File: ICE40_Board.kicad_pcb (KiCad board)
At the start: 4 copper layers, 62.5 x 26.7 mm, 40 parts, among them J1 SPI, J2 EXPANSION, J3 R_HDR, J4 L_HDR, U1 AZ1117-1.2, U2 AMS1117-3.3, U3 USB4110-GF-A, U4 iCE40HX1K-VQ100, U5 FT2232HQ, U6 93LCxxC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

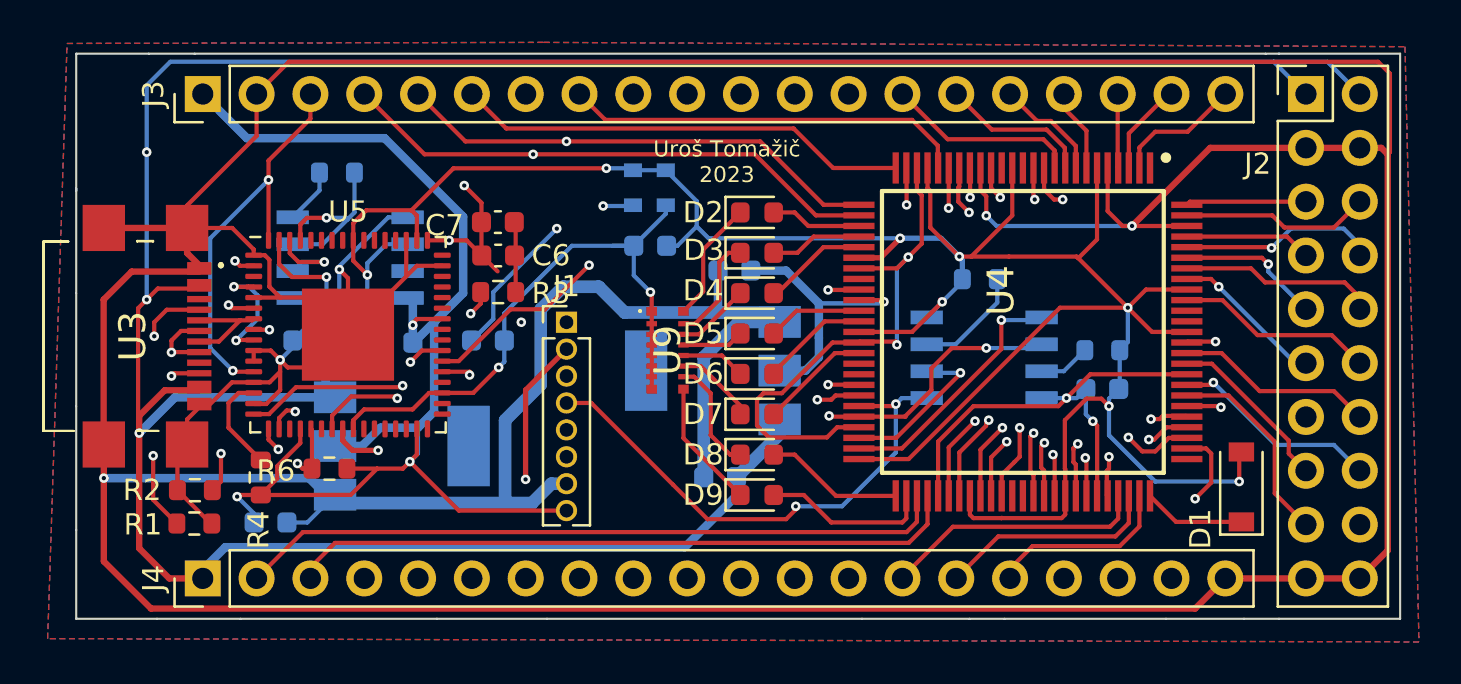
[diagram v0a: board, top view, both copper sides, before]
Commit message: added power led
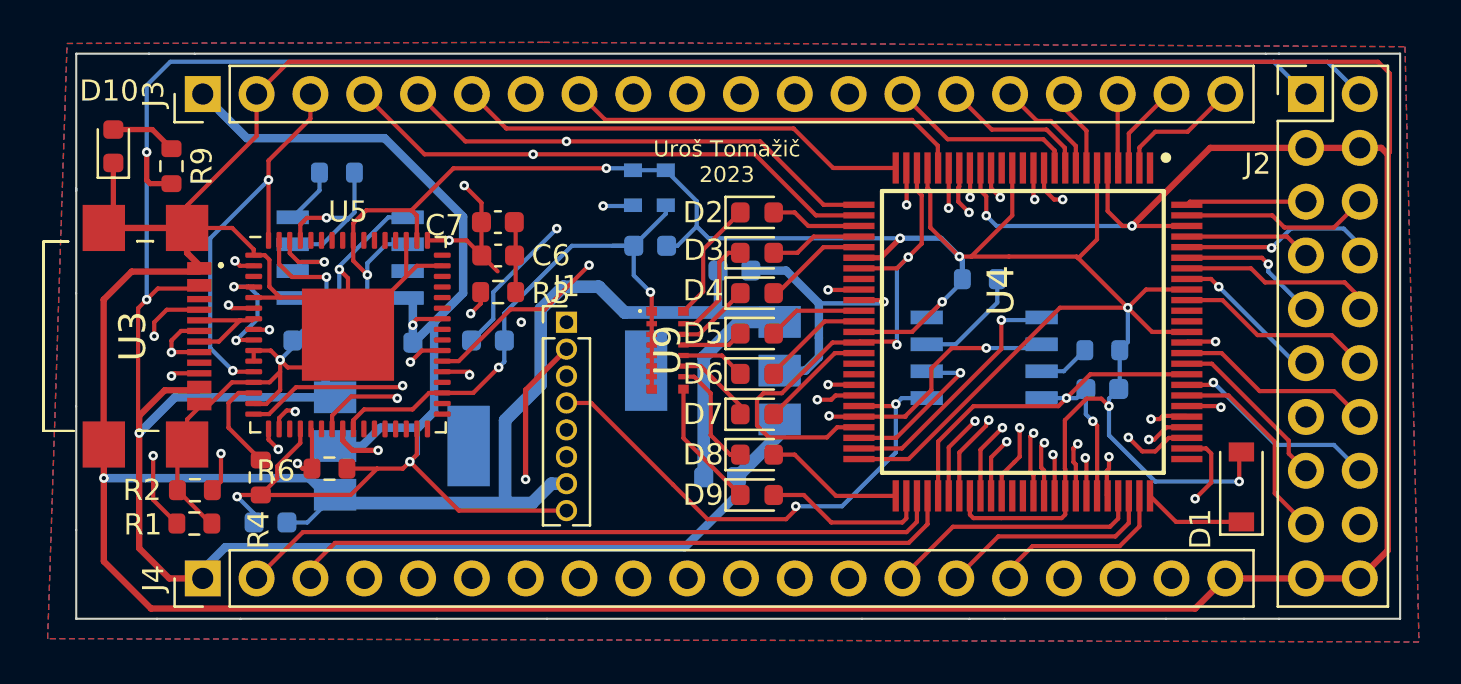
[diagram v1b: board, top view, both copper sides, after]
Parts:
- added D10: LED, LED_SMD:LED_0603_1608Metric, F.Cu at (68.9, 46.2)
- added R9: 330R, Resistor_SMD:R_0603_1608Metric, F.Cu at (71.7, 47.1)
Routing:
- net GND: track 413.6 -> 416.8 mm
- net Net-(D10-Pad2): track 0.00 -> 3.12 mm
- net +5V: track 164.3 -> 166.8 mm
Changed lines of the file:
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@@
   (net 131 "unconnected-(U6-Pad7)")
   (net 132 "Net-(C6-Pad2)")
+  (net 133 "Net-(D10-Pad2)")
   (footprint "Diode_SMD:D_SOD-123" (layer "F.Cu")
     (at 122.174 62.23 90)
@@
     )
   )
+  (footprint "Resistor_SMD:R_0603_1608Metric" (layer "F.Cu")
+    (at 71.6788 47.0916 -90)
+    (descr "Resistor SMD 0603 (1608 Metric), square (rectangular) end terminal, IPC_7351 nominal, (Body size source: IPC-SM-782 page 72, https://www.pcb-3d.com/wordpress/wp-content/uploads/ipc-sm-782a_amendment_1_and_2.pdf), generated with kicad-footprint-generator")
+    (tags "resistor")
+    (property "Sheetfile" "ICE40_Board.kicad_sch")
+    (property "Sheetname" "")
+    (attr smd)
+    (fp_text reference "R9" (at 0 -1.43 90) (layer "F.SilkS")
+      (effects (font (size 1 1) (thickness 0.15)))
+    )
+    (fp_text value "330R" (at 0 1.43 90) (layer "F.Fab")
+      (effects (font (size 1 1) (thickness 0.15)))
+    )
+    (fp_text user "${REFERENCE}" (at 0 0 90) (layer "F.Fab")
+      (effects (font (size 0.4 0.4) (thickness 0.06)))
+    )
+    (fp_line (start -0.237258 0.5225) (end 0.237258 0.5225) (layer "F.SilkS") (width 0.12))
+    (fp_line (start -0.237258 -0.5225) (end 0.237258 -0.5225) (layer "F.SilkS") (width 0.12))
+    (fp_line (start 1.48 0.73) (end -1.48 0.73) (layer "F.CrtYd") (width 0.05))
+    (fp_line (start 1.48 -0.73) (end 1.48 0.73) (layer "F.CrtYd") (width 0.05))
+    (fp_line (start -1.48 -0.73) (end 1.48 -0.73) (layer "F.CrtYd") (width 0.05))
+    (fp_line (start -1.48 0.73) (end -1.48 -0.73) (layer "F.CrtYd") (width 0.05))
+    (fp_line (start -0.8 -0.4125) (end 0.8 -0.4125) (layer "F.Fab") (width 0.1))
+    (fp_line (start 0.8 -0.4125) (end 0.8 0.4125) (layer "F.Fab") (width 0.1))
+    (fp_line (start -0.8 0.4125) (end -0.8 -0.4125) (layer "F.Fab") (width 0.1))
+    (fp_line (start 0.8 0.4125) (end -0.8 0.4125) (layer "F.Fab") (width 0.1))
+    (pad "1" smd roundrect (at -0.825 0 270) (size 0.8 0.95) (layers "F.Cu" "F.Paste" "F.Mask") (roundrect_rratio 0.25)
+      (net 133 "Net-(D10-Pad2)") (pintype "passive"))
+    (pad "2" smd roundrect (at 0.825 0 270) (size 0.8 0.95) (layers "F.Cu" "F.Paste" "F.Mask") (roundrect_rratio 0.25)
+      (net 3 "+5V") (pintype "passive"))
+    (model "${KICAD6_3DMODEL_DIR}/Resistor_SMD.3dshapes/R_0603_1608Metric.wrl"
+      (offset (xyz 0 0 0))
+      (scale (xyz 1 1 1))
+      (rotate (xyz 0 0 0))
+    )
+  )
   (footprint "LED_SMD:LED_0603_1608Metric" (layer "F.Cu")
     (at 99.314 62.611)
@@
     )
   )
+  (footprint "LED_SMD:LED_0603_1608Metric" (layer "F.Cu")
+    (at 68.9356 46.1519 90)
+    (descr "LED SMD 0603 (1608 Metric), square (rectangular) end terminal, IPC_7351 nominal, (Body size source: http://www.tortai-tech.com/upload/download/2011102023233369053.pdf), generated with kicad-footprint-generator")
+    (tags "LED")
+    (property "Sheetfile" "ICE40_Board.kicad_sch")
+    (property "Sheetname" "")
+    (attr smd)
+    (fp_text reference "D10" (at 2.6163 -0.2032 180) (layer "F.SilkS")
+      (effects (font (size 1 1) (thickness 0.15)))
+    )
+    (fp_text value "LED" (at 0 1.43 90) (layer "F.Fab")
+      (effects (font (size 1 1) (thickness 0.15)))
+    )
+    (fp_text user "${REFERENCE}" (at 0 0 90) (layer "F.Fab")
+      (effects (font (size 0.4 0.4) (thickness 0.06)))
+    )
+    (fp_line (start -1.485 0.735) (end 0.8 0.735) (layer "F.SilkS") (width 0.12))
+    (fp_line (start 0.8 -0.735) (end -1.485 -0.735) (layer "F.SilkS") (width 0.12))
+    (fp_line (start -1.485 -0.735) (end -1.485 0.735) (layer "F.SilkS") (width 0.12))
+    (fp_line (start -1.48 -0.73) (end 1.48 -0.73) (layer "F.CrtYd") (width 0.05))
+    (fp_line (start 1.48 -0.73) (end 1.48 0.73) (layer "F.CrtYd") (width 0.05))
+    (fp_line (start -1.48 0.73) (end -1.48 -0.73) (layer "F.CrtYd") (width 0.05))
+    (fp_line (start 1.48 0.73) (end -1.48 0.73) (layer "F.CrtYd") (width 0.05))
+    (fp_line (start -0.5 -0.4) (end -0.8 -0.1) (layer "F.Fab") (width 0.1))
+    (fp_line (start -0.8 -0.1) (end -0.8 0.4) (layer "F.Fab") (width 0.1))
+    (fp_line (start 0.8 -0.4) (end -0.5 -0.4) (layer "F.Fab") (width 0.1))
+    (fp_line (start 0.8 0.4) (end 0.8 -0.4) (layer "F.Fab") (width 0.1))
+    (fp_line (start -0.8 0.4) (end 0.8 0.4) (layer "F.Fab") (width 0.1))
+    (pad "1" smd roundrect (at -0.7875 0 90) (size 0.875 0.95) (layers "F.Cu" "F.Paste" "F.Mask") (roundrect_rratio 0.25)
+      (net 2 "GND") (pinfunction "K") (pintype "passive"))
+    (pad "2" smd roundrect (at 0.7875 0 90) (size 0.875 0.95) (layers "F.Cu" "F.Paste" "F.Mask") (roundrect_rratio 0.25)
+      (net 133 "Net-(D10-Pad2)") (pinfunction "A") (pintype "passive"))
+    (model "${KICAD6_3DMODEL_DIR}/LED_SMD.3dshapes/LED_0603_1608Metric.wrl"
+      (offset (xyz 0 0 0))
+      (scale (xyz 1 1 1))
+      (rotate (xyz 0 0 0))
+    )
+  )
   (footprint "Package_TO_SOT_SMD:SOT-223" (layer "B.Cu")
     (at 97.2312 56.7436 180)
@@
     (effects (font (size 0.75 0.75) (thickness 0.15)))
   )
-  (segment (start 107.974 53.4148) (end 108.0545 53.4953) (width 0.25) (layer "F.Cu") (net 1))
   (segment (start 83.26 60.7072) (end 83.26 59.494) (width 0.2) (layer "F.Cu") (net 1))
   (segment (start 80.26 50.594) (end 80.26 49.788) (width 0.2) (layer "F.Cu") (net 1))
@@
   (segment (start 117.9576 54.9148) (end 116.8146 53.7718) (width 0.2) (layer "F.Cu") (net 1))
   (segment (start 119.5996 54.9148) (end 117.9576 54.9148) (width 0.2) (layer "F.Cu") (net 1))
-  (segment (start 110.8616 63.6872) (end 110.8456 63.7032) (width 0.2) (layer "F.Cu") (net 1))
   (segment (start 113.8616 62.6528) (end 113.8616 63.532) (width 0.2) (layer "F.Cu") (net 1))
   (segment (start 74.754 55.294) (end 74.7268 55.3212) (width 0.2) (layer "F.Cu") (net 1))
@@
   (segment (start 120.7008 46.228) (end 117.014 49.9148) (width 0.3) (layer "F.Cu") (net 2))
   (segment (start 119.9946 67.9704) (end 121.417 66.548) (width 0.3) (layer "F.Cu") (net 2))
+  (segment (start 68.9356 49.5589) (end 68.4865 50.008) (width 0.25) (layer "F.Cu") (net 2))
   (segment (start 73.5828 63.9572) (end 73.534 63.9572) (width 0.2) (layer "F.Cu") (net 2))
   (segment (start 76.8096 56.2356) (end 77.1652 56.5912) (width 0.2) (layer "F.Cu") (net 2))
@@
   (segment (start 68.4865 60.228) (end 68.4865 61.8155) (width 0.3) (layer "F.Cu") (net 2))
   (segment (start 107.8616 62.6528) (end 107.8616 60.089394) (width 0.2) (layer "F.Cu") (net 2))
+  (segment (start 68.9356 46.9394) (end 68.9356 49.5589) (width 0.25) (layer "F.Cu") (net 2))
   (segment (start 72.9915 52.068) (end 69.8012 52.068) (width 0.3) (layer "F.Cu") (net 2))
   (segment (start 78.4628 56.5912) (end 80.01 55.044) (width 0.2) (layer "F.Cu") (net 2))
@@
   (segment (start 70.5104 53.3908) (end 70.104 53.7972) (width 0.2) (layer "F.Cu") (net 3))
   (segment (start 70.104 58.8264) (end 70.1548 58.8772) (width 0.2) (layer "F.Cu") (net 3))
+  (segment (start 71.6788 47.9166) (end 70.675 47.9166) (width 0.25) (layer "F.Cu") (net 3))
+  (segment (start 70.675 47.9166) (end 70.5104 47.752) (width 0.25) (layer "F.Cu") (net 3))
+  (segment (start 70.5104 47.752) (end 70.5104 46.4312) (width 0.25) (layer "F.Cu") (net 3))
   (segment (start 72.9915 57.668) (end 71.364 57.668) (width 0.3) (layer "F.Cu") (net 3))
   (segment (start 70.104 53.7972) (end 70.104 58.8264) (width 0.2) (layer "F.Cu") (net 3))
@@
   (segment (start 107.3208 58.039) (end 106.1466 58.039) (width 0.2) (layer "B.Cu") (net 26))
   (segment (start 103.3272 63.1444) (end 105.8672 60.6044) (width 0.2) (layer "B.Cu") (net 26))
-  (segment (start 90.3224 58.2676) (end 90.7796 58.2676) (width 0.2) (layer "B.Cu") (net 26))
   (segment (start 106.1466 58.039) (end 105.8672 58.3184) (width 0.2) (layer "B.Cu") (net 26))
   (segment (start 105.8672 60.6044) (end 105.8672 58.3184) (width 0.2) (layer "B.Cu") (net 26))
@@
   (segment (start 87.9222 49.7962) (end 87.8592 49.7332) (width 0.2) (layer "F.Cu") (net 132))
   (segment (start 87.9222 53.0352) (end 87.9222 49.7962) (width 0.2) (layer "F.Cu") (net 132))
+  (segment (start 68.9356 45.3644) (end 70.7766 45.3644) (width 0.25) (layer "F.Cu") (net 133))
+  (segment (start 70.7766 45.3644) (end 71.6788 46.2666) (width 0.25) (layer "F.Cu") (net 133))
   (zone (net 2) (net_name "GND") (layers "F.Cu" "In1.Cu" "In2.Cu" "B.Cu") (hatch edge 0.508)
     (connect_pads (clearance 0.508))

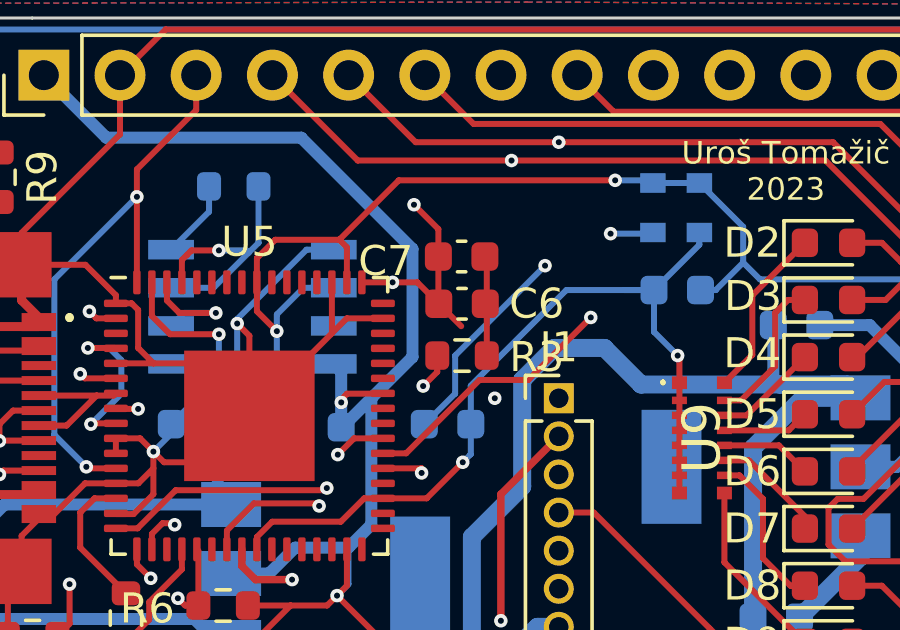
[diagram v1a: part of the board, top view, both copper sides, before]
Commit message: added led
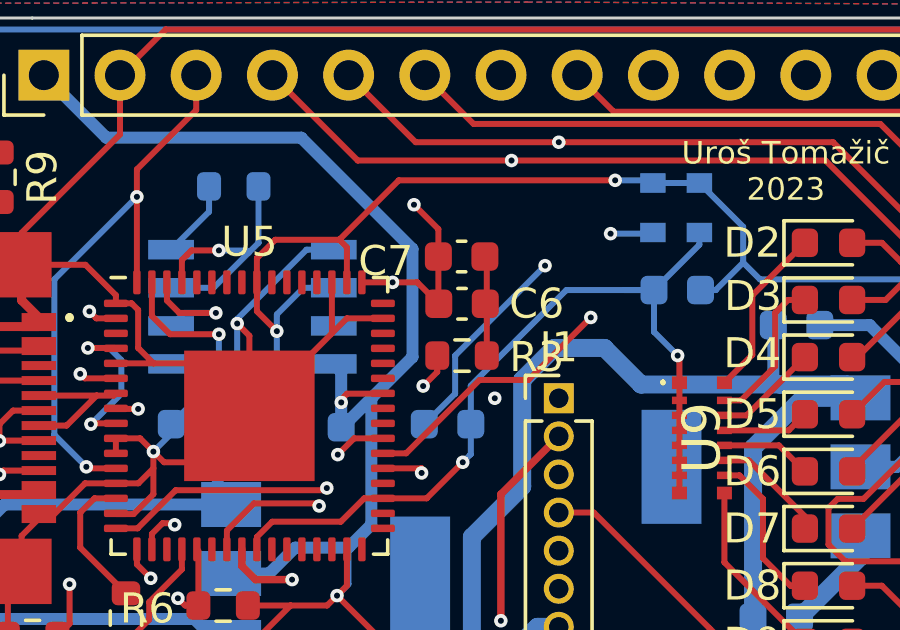
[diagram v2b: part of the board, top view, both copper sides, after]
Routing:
- net +1V8: track 48.8 -> 47.7 mm
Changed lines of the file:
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@@
   (segment (start 86.3092 48.8188) (end 85.4964 48.006) (width 0.2) (layer "F.Cu") (net 4))
   (segment (start 86.3092 49.7332) (end 86.3092 48.8188) (width 0.2) (layer "F.Cu") (net 4))
-  (segment (start 87.0712 52.057) (end 86.3222 51.308) (width 0.2) (layer "F.Cu") (net 4))
   (segment (start 78.237 43.688) (end 78.237 44.8514) (width 0.2) (layer "F.Cu") (net 4))
   (segment (start 83.76 50.594) (end 84.7824 50.594) (width 0.2) (layer "F.Cu") (net 4))
@@
   (segment (start 90.3224 46.736) (end 91.2876 47.7012) (width 0.2) (layer "In1.Cu") (net 117))
   (segment (start 91.3892 51.6128) (end 91.3892 51.7652) (width 0.2) (layer "In1.Cu") (net 117))
-  (segment (start 91.3892 51.7652) (end 91.3892 51.9684) (width 0.2) (layer "In1.Cu") (net 117))
   (segment (start 91.2876 47.7012) (end 91.3892 47.8028) (width 0.2) (layer "In1.Cu") (net 117))
   (segment (start 91.3892 47.8028) (end 91.3892 51.6128) (width 0.2) (layer "In1.Cu") (net 117))
